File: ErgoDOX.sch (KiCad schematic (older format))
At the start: 83 parts, among them J1 SPLIT_JACK_TOP, J2 EXT1_TOP, J3 EXT1_BOT, J4 EXT1_TOP2, J5 SPLIT_JACK_BOT, J6 USB_C_TOP, J7 USB_C_BOT, J8 Conn_ARM_JTAG_SWD_10, J9 Conn_01x04, SW0:10 SW0:3, SW0:11 SW0:2, SW0:12 SW0:1, SW0:7 SW0:6, SW0:8 SW0:5, SW0:9 SW0:4, SW1:10 SW1:3, SW1:11 SW1:2, SW1:12 SW1:1, SW1:13 SW1:0, SW1:9 SW1:4, SW2:10 SW2:3, SW2:11 SW2:2, SW2:12 SW2:1, SW2:13 SW2:0, SW2:7 SW2:6, SW2:8 SW2:5, SW2:9 SW2:4, SW3:10 SW3:3, SW3:11 SW3:2, SW3:12 SW3:1, SW3:13 SW3:0, SW3:8 SW3:5, SW3:9 SW3:4, SW4:10 SW4:3, SW4:11 SW4:2, SW4:12 SW4:1, SW4:13 SW4:0, SW4:7 SW4:6, SW4:8 SW4:5, SW4:9 SW4:4, SW5:10 SW5:3, SW5:11 SW5:2, SW5:12 SW5:1, SW5:13 SW5:0, SW5:7 SW5:6, SW5:8 SW5:5, SW5:9 SW5:4, U1 STM32F072C8Tx, U2 MCP1700-1202E_SOT23

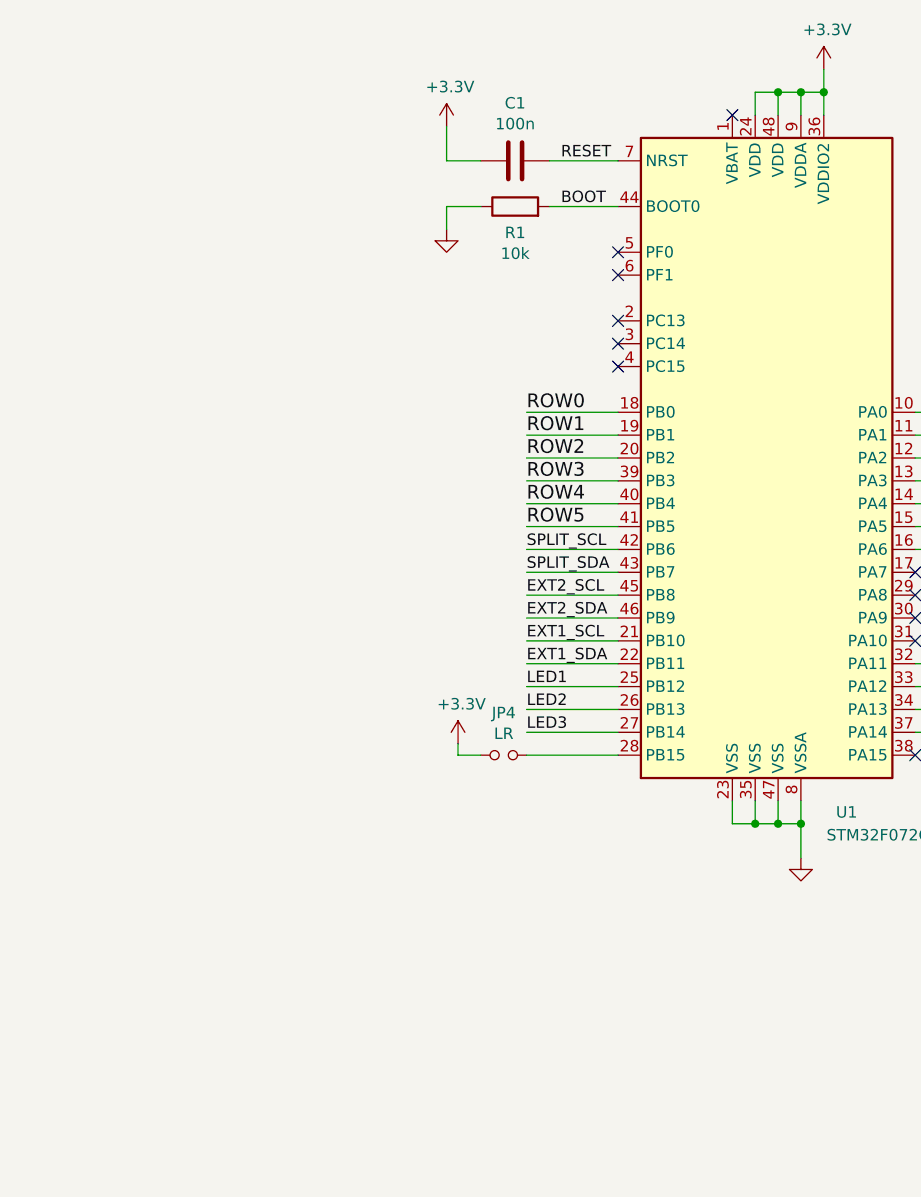
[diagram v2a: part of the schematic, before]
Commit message: Add testpoints and fix some stuff.
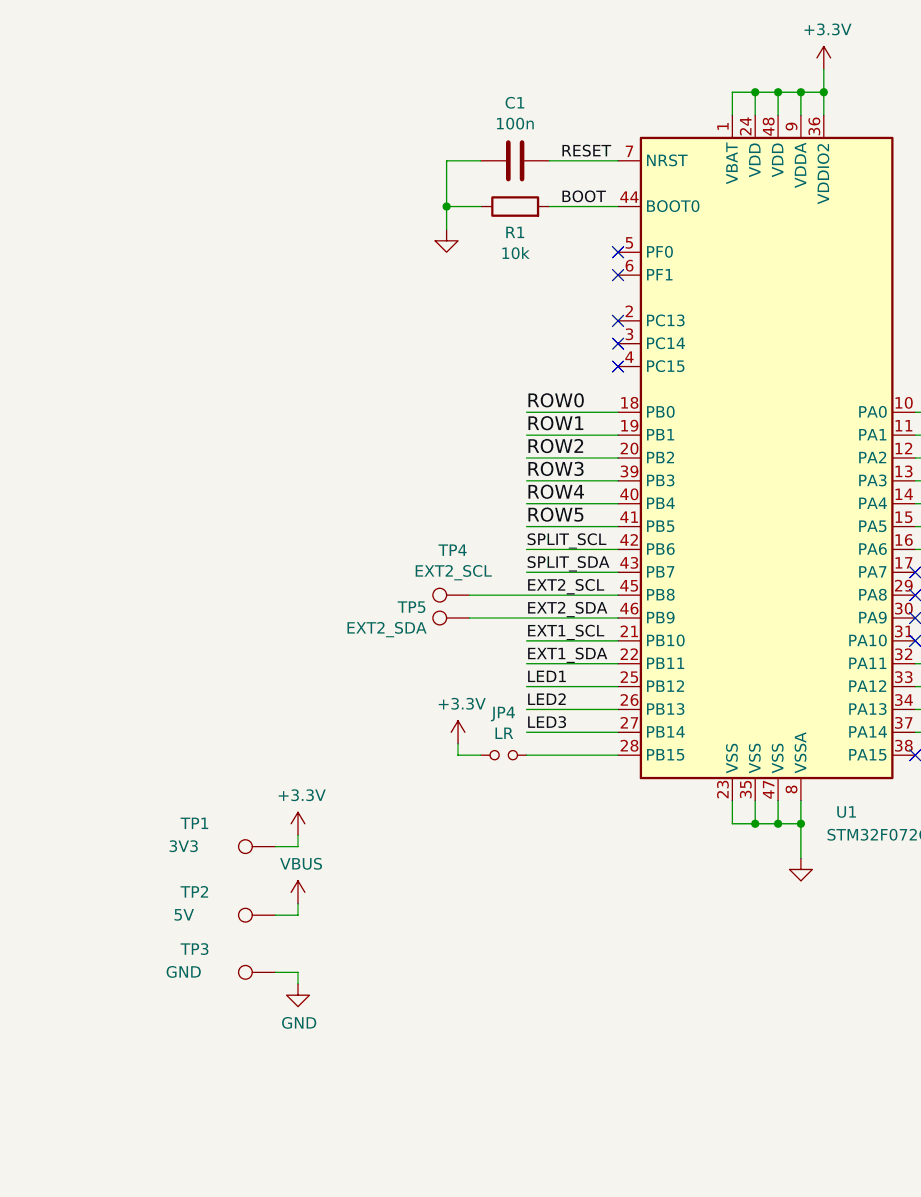
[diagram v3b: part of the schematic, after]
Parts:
- added TP1: 3V3, TestPoint:TestPoint_Pad_D1.5mm, symbol Connector:TestPoint
- added TP2: 5V, TestPoint:TestPoint_Pad_D1.5mm, symbol Connector:TestPoint
- added TP3: GND, TestPoint:TestPoint_Pad_D1.5mm, symbol Connector:TestPoint
- added TP4: EXT2_SCL, TestPoint:TestPoint_Pad_D1.5mm, symbol Connector:TestPoint
- added TP5: EXT2_SDA, TestPoint:TestPoint_Pad_D1.5mm, symbol Connector:TestPoint
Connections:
- net +3V3: now also U1.1 (VBAT), TP1.1; no longer C1.2
- net EXT2_SCL: now also TP4.1
- net EXT2_SDA: now also TP5.1
- net GND: now also C1.2, TP3.1
- net VBUS: now also TP2.1
- no-connect marks 21 -> 20
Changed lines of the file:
@@
 Text Label 9950 3400 0    50   ~ 0
 EXT1_SCL
-Wire Wire Line
-	10350 3200 9950 3200
 Text Label 9950 3200 0    50   ~ 0
 EXT2_SCL
@@
 NoConn ~ 10350 2100
 NoConn ~ 10350 2200
-$Comp
-L power:+3.3V #PWR0106
-U 1 1 5F45EBC1
-P 9600 1150
-F 0 "#PWR0106" H 9600 1000 50  0001 C CNN
-F 1 "+3.3V" H 9615 1323 50  0000 C CNN
-F 2 "" H 9600 1150 50  0001 C CNN
-F 3 "" H 9600 1150 50  0001 C CNN
-	1    9600 1150
-	1    0    0    -1
-$EndComp
-Wire Wire Line
-	9750 1300 9600 1300
-Wire Wire Line
-	9600 1300 9600 1150
 Text Label 10100 1500 0    50   ~ 0
 BOOT
@@
 	10950 1000 11050 1000
 Connection ~ 11050 1000
-NoConn ~ 10850 1100
 $Comp
 L power:+3.3V #PWR0107
@@
 NoConn ~ 10650 7450
 Wire Wire Line
-	10350 3300 9950 3300
-Wire Wire Line
 	10350 3400 9950 3400
 Wire Wire Line
@@
 	0    1    1    0
 $EndComp
+Wire Wire Line
+	10850 1100 10850 1000
+Wire Wire Line
+	10850 1000 10950 1000
+Connection ~ 10950 1000
+Wire Wire Line
+	9750 1300 9600 1300
+Wire Wire Line
+	9600 1300 9600 1500
+Connection ~ 9600 1500
+$Comp
+L Connector:TestPoint TP4
+U 1 1 5F29F4CD
+P 9700 3200
+F 0 "TP4" V 9895 3272 50  0000 C CNN
+F 1 "EXT2_SCL" V 9804 3272 50  0000 C CNN
+F 2 "TestPoint:TestPoint_Pad_D1.5mm" H 9900 3200 50  0001 C CNN
+F 3 "~" H 9900 3200 50  0001 C CNN
+	1    9700 3200
+	0    -1   -1   0
+$EndComp
+$Comp
+L Connector:TestPoint TP5
+U 1 1 5F2A08F4
+P 9700 3300
+F 0 "TP5" V 9746 3487 50  0000 L CNN
+F 1 "EXT2_SDA" V 9655 3487 50  0000 L CNN
+F 2 "TestPoint:TestPoint_Pad_D1.5mm" H 9900 3300 50  0001 C CNN
+F 3 "~" H 9900 3300 50  0001 C CNN
+	1    9700 3300
+	0    -1   -1   0
+$EndComp
+Wire Wire Line
+	9700 3200 10350 3200
+Wire Wire Line
+	9700 3300 10350 3300
+$Comp
+L Connector:TestPoint TP1
+U 1 1 5F2F1100
+P 8850 4300
+F 0 "TP1" V 8950 4650 50  0000 C CNN
+F 1 "3V3" V 8850 4700 50  0000 C CNN
+F 2 "TestPoint:TestPoint_Pad_D1.5mm" H 9050 4300 50  0001 C CNN
+F 3 "~" H 9050 4300 50  0001 C CNN
+	1    8850 4300
+	0    -1   -1   0
+$EndComp
+Wire Wire Line
+	8850 4300 8950 4300
+Wire Wire Line
+	8950 4300 8950 4250
+$Comp
+L power:+3.3V #PWR0106
+U 1 1 5F31C7B2
+P 8950 4250
+F 0 "#PWR0106" H 8950 4100 50  0001 C CNN
+F 1 "+3.3V" H 8965 4423 50  0000 C CNN
+F 2 "" H 8950 4250 50  0001 C CNN
+F 3 "" H 8950 4250 50  0001 C CNN
+	1    8950 4250
+	1    0    0    -1
+$EndComp
+$Comp
+L Connector:TestPoint TP2
+U 1 1 5F31C86F
+P 8850 4600
+F 0 "TP2" V 8950 4950 50  0000 C CNN
+F 1 "5V" V 8850 5000 50  0000 C CNN
+F 2 "TestPoint:TestPoint_Pad_D1.5mm" H 9050 4600 50  0001 C CNN
+F 3 "~" H 9050 4600 50  0001 C CNN
+	1    8850 4600
+	0    -1   -1   0
+$EndComp
+Wire Wire Line
+	8850 4600 8950 4600
+Wire Wire Line
+	8950 4600 8950 4550
+$Comp
+L power:VBUS #PWR0134
+U 1 1 5F346AB4
+P 8950 4550
+F 0 "#PWR0134" H 8950 4400 50  0001 C CNN
+F 1 "VBUS" H 8965 4723 50  0000 C CNN
+F 2 "" H 8950 4550 50  0001 C CNN
+F 3 "" H 8950 4550 50  0001 C CNN
+	1    8950 4550
+	1    0    0    -1
+$EndComp
+$Comp
+L Connector:TestPoint TP3
+U 1 1 5F346F91
+P 8850 4850
+F 0 "TP3" V 8950 5200 50  0000 C CNN
+F 1 "GND" V 8850 5250 50  0000 C CNN
+F 2 "TestPoint:TestPoint_Pad_D1.5mm" H 9050 4850 50  0001 C CNN
+F 3 "~" H 9050 4850 50  0001 C CNN
+	1    8850 4850
+	0    -1   -1   0
+$EndComp
+Wire Wire Line
+	8850 4850 8950 4850
+Wire Wire Line
+	8950 4850 8950 4900
+$Comp
+L power:GND #PWR0135
+U 1 1 5F466568
+P 8950 4900
+F 0 "#PWR0135" H 8950 4650 50  0001 C CNN
+F 1 "GND" H 8955 4727 50  0000 C CNN
+F 2 "" H 8950 4900 50  0001 C CNN
+F 3 "" H 8950 4900 50  0001 C CNN
+	1    8950 4900
+	1    0    0    -1
+$EndComp
 $EndSCHEMATC
